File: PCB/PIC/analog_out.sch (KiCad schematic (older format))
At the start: 27 parts, among them J19 TB_1X2, Q1 PBSS5240XF, Q14 BC817-40, U18 LM358, U21 MCP6022

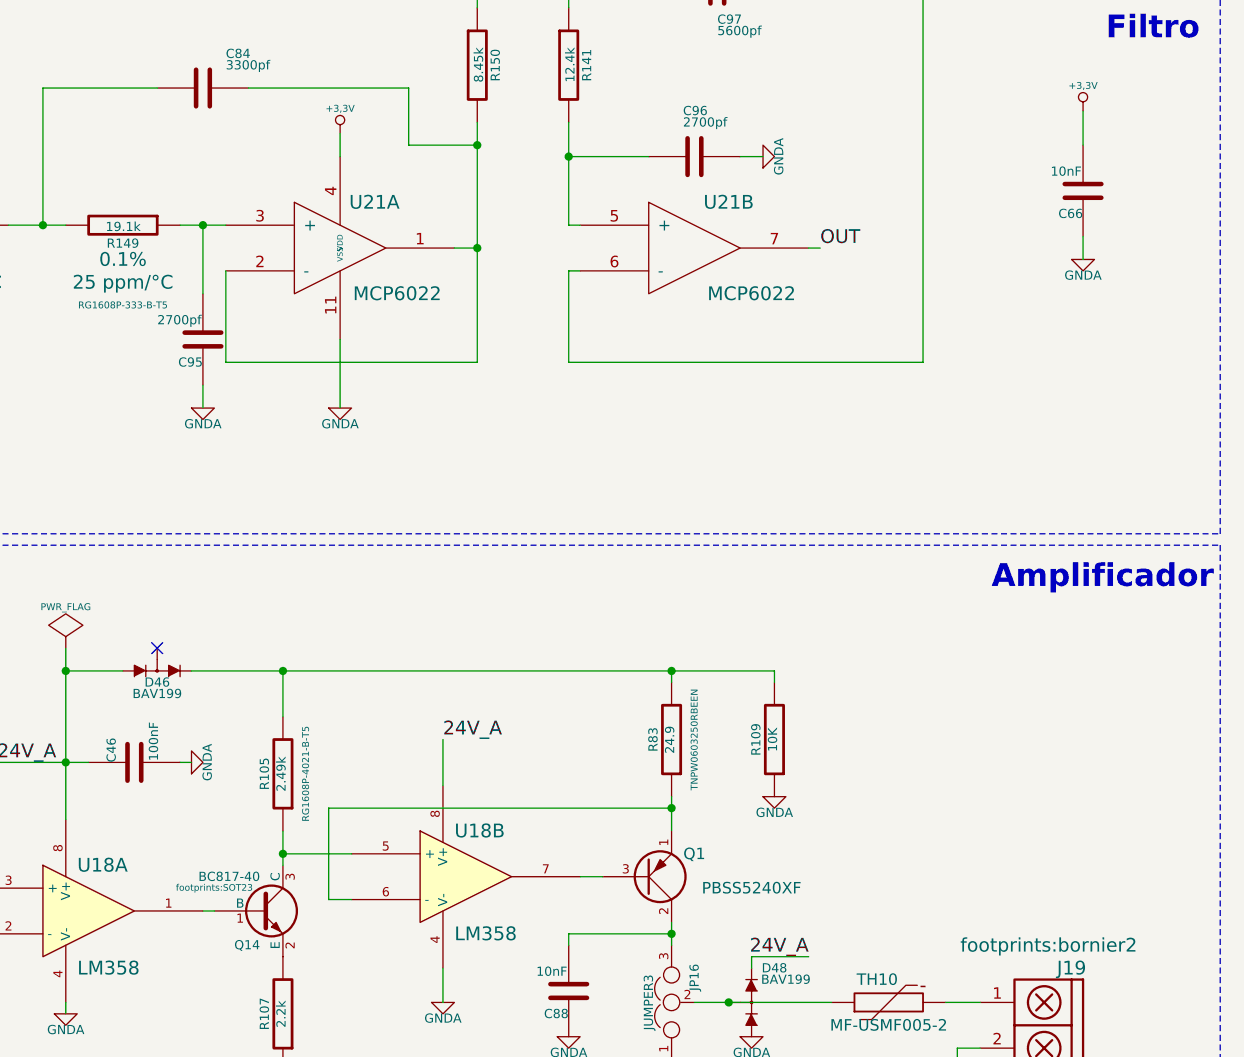
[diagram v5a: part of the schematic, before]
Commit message: rev02 se completa campo num. de frabicante(#manf) CIAA-PIC
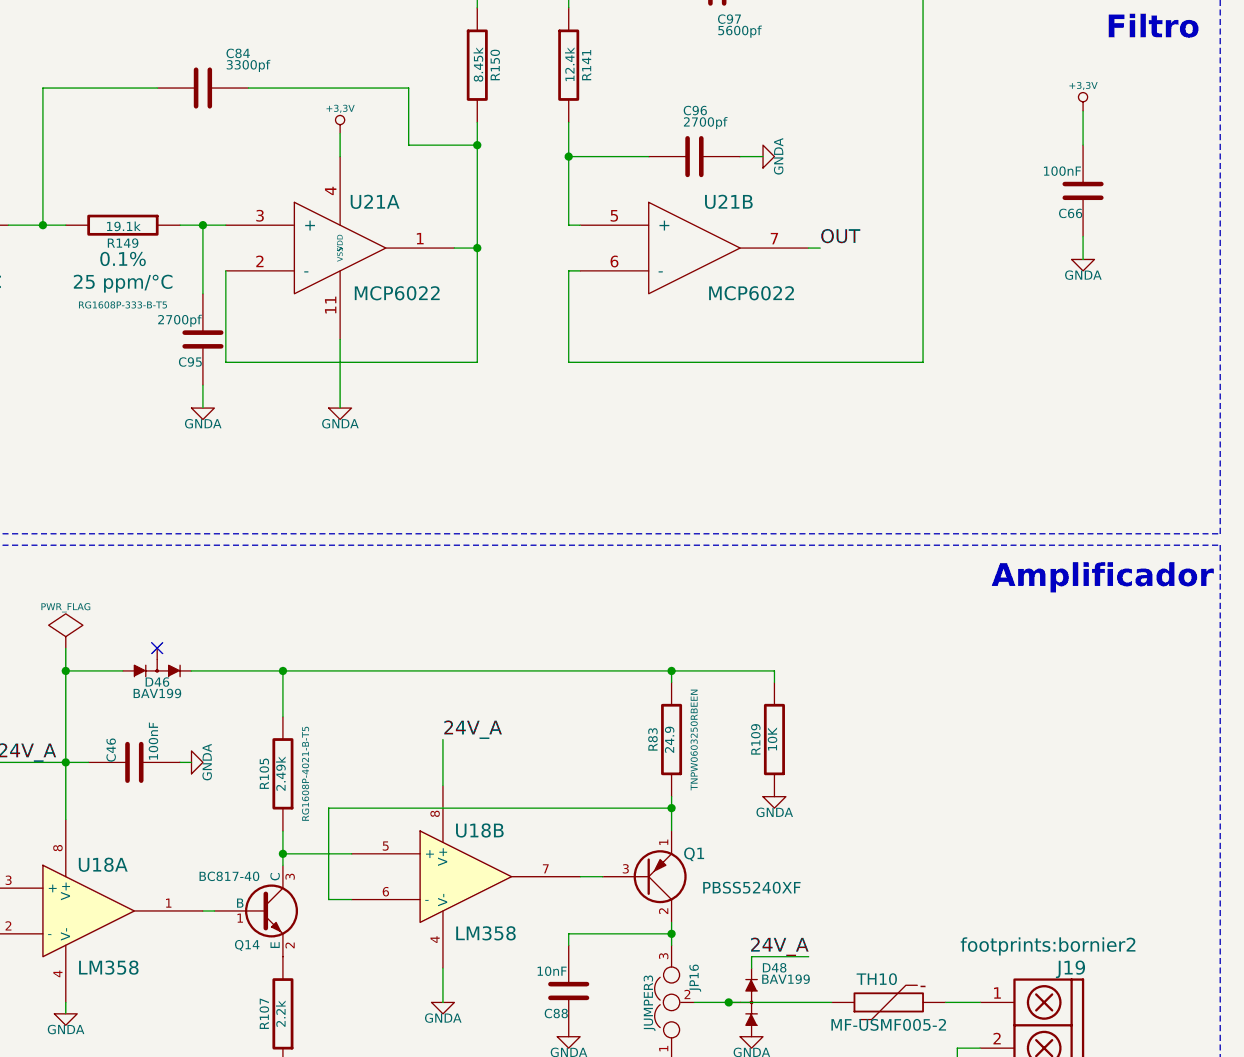
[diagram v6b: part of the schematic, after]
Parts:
- C46: #manf (none) -> C0603C104K5RACTU
- C66: value 10nF -> 100nF; #manf (none) -> C0603C104K5RACTU
- C88: #manf (none) -> C0603C103K5RACTU
- D46: footprint (none) -> footprints:SOT23-DIODE; #manf (none) -> BAV199LT1G
- D48: footprint (none) -> footprints:-SOT89; #manf (none) -> BAV199LT1G
- FB21: footprint (none) -> footprints:SM0603; #manf (none) -> MMZ1608B601CTAH0
- J19: #manf (none) -> OSTTC022162
- JP16: footprint (none) -> footprints:GS3
- Q1: footprint (none) -> footprints:-SOT89; #manf (none) -> PBSS5240XF
- Q14: #manf (none) -> BC817-40LT3G
- R105, R83: #manf (none) -> ERA-3AEB2491V
- R107: footprint Resistors_SMD:R_0603 -> Resistors_SMD:R_1206; #manf (none) -> ERJ-8GEYJ222V
- R109: #manf (none) -> RC0603JR-0710KL
- R80: #manf (none) -> ERA-3AEB333V
- R82: #manf (none) -> RG1608P-153-B-T5
- TH10: footprint (none) -> footprints:MF-USMF; #manf (none) -> MF-USMF005-2
- U18: footprint (none) -> SMD_Packages:SOIC-8-N; #manf (none) -> LM358DG
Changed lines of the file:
@@
 $EndDescr
 $Comp
-L +24V #PWR0157
+L +24V #PWR0158
 U 1 1 532CCE3B
 P 3600 4150
-F 0 "#PWR0157" H 3600 4100 20  0001 C CNN
+F 0 "#PWR0158" H 3600 4100 20  0001 C CNN
 F 1 "+24V" H 3600 4250 30  0000 C CNN
 F 2 "" H 3600 4150 60  0000 C CNN
@@
 F 2 "Capacitors_SMD:C_0603" H 5038 4050 30  0001 C CNN
 F 3 "~" H 5000 4200 60  0000 C CNN
+F 4 "C0603C104K5RACTU" H 5000 4200 60  0001 C CNN "#manf"
 	1    5000 4200
 	0    -1   -1   0
 $EndComp
 $Comp
-L GNDA-RESCUE-ciaa-pic #PWR0158
+L GNDA-RESCUE-ciaa-pic #PWR0159
 U 1 1 532CFB46
 P 4700 5300
-F 0 "#PWR0158" H 4700 5300 40  0001 C CNN
+F 0 "#PWR0159" H 4700 5300 40  0001 C CNN
 F 1 "GNDA" H 4700 5230 40  0000 C CNN
 F 2 "" H 4700 5300 60  0000 C CNN
@@
 $EndComp
 $Comp
-L GNDA-RESCUE-ciaa-pic #PWR0159
+L GNDA-RESCUE-ciaa-pic #PWR0160
 U 1 1 532CFB6F
 P 5250 4200
-F 0 "#PWR0159" H 5250 4200 40  0001 C CNN
+F 0 "#PWR0160" H 5250 4200 40  0001 C CNN
 F 1 "GNDA" H 5250 4130 40  0000 C CNN
 F 2 "" H 5250 4200 60  0000 C CNN
@@
 F 4 "0.1%" V 4900 5600 60  0000 C CNN "Tol"
 F 5 "25 ppm/°C" V 5000 5600 60  0000 C CNN "TC"
+F 6 "ERA-3AEB333V" V 4750 5600 60  0001 C CNN "#manf"
 	1    4750 5600
 	0    1    1    0
@@
 F 4 "0.1%" V 4150 5950 60  0000 C CNN "Tol"
 F 5 "25 ppm/°C" V 4250 5950 60  0000 C CNN "TC"
+F 6 "RG1608P-153-B-T5" V 4000 5950 60  0001 C CNN "#manf"
 	1    4000 5950
 	-1   0    0    1
 $EndComp
 $Comp
-L GNDA-RESCUE-ciaa-pic #PWR0160
+L GNDA-RESCUE-ciaa-pic #PWR0161
 U 1 1 532D06E5
 P 4000 6250
-F 0 "#PWR0160" H 4000 6250 40  0001 C CNN
+F 0 "#PWR0161" H 4000 6250 40  0001 C CNN
 F 1 "GNDA" H 4000 6180 40  0000 C CNN
 F 2 "" H 4000 6250 60  0000 C CNN
@@
 F 0 "U18" H 4750 5050 60  0000 L CNN
 F 1 "LM358" H 4750 4600 60  0000 L CNN
-F 2 "" H 4800 4850 60  0001 C CNN
+F 2 "SMD_Packages:SOIC-8-N" H 4800 4850 60  0001 C CNN
 F 3 "" H 4800 4850 60  0000 C CNN
+F 4 "LM358DG " H 4800 4850 60  0001 C CNN "#manf"
 	1    4800 4850
 	1    0    0    -1
@@
 F 2 "footprints:bornier2" H 9100 5700 60  0000 C CNN
 F 3 "~" H 9000 5400 60  0000 C CNN
+F 4 "OSTTC022162" H 9050 5350 60  0001 C CNN "#manf"
 	1    9050 5350
 	-1   0    0    -1
 $EndComp
 $Comp
-L GNDA-RESCUE-ciaa-pic #PWR0161
+L GNDA-RESCUE-ciaa-pic #PWR0162
 U 1 1 532A8008
 P 8600 5500
-F 0 "#PWR0161" H 8600 5500 40  0001 C CNN
+F 0 "#PWR0162" H 8600 5500 40  0001 C CNN
 F 1 "GNDA" H 8600 5430 40  0000 C CNN
 F 2 "" H 8600 5500 60  0000 C CNN
@@
 F 0 "FB21" H 4000 4350 60  0000 C CNN
 F 1 "MMZ1608B601C" H 4000 4100 60  0000 C CNN
-F 2 "" H 4000 4200 60  0001 C CNN
+F 2 "footprints:SM0603" H 4000 4200 60  0001 C CNN
 F 3 "~" H 4000 4200 60  0000 C CNN
+F 4 "MMZ1608B601CTAH0" H 4000 4200 60  0001 C CNN "#manf"
 	1    4000 4200
 	1    0    0    -1
 $EndComp
 $Comp
-L PWR_FLAG #FLG0162
+L PWR_FLAG #FLG0163
 U 1 1 532B208A
 P 4700 3700
-F 0 "#FLG0162" H 4700 3795 30  0001 C CNN
+F 0 "#FLG0163" H 4700 3795 30  0001 C CNN
 F 1 "PWR_FLAG" H 4700 3880 30  0000 C CNN
 F 2 "" H 4700 3700 60  0000 C CNN
@@
 F 0 "Q14" H 5550 4701 40  0000 R CNN
 F 1 "BC817-40" H 5550 5000 40  0000 R CNN
-F 2 "footprints:SOT23" H 5350 4952 29  0000 C CNN
+F 2 "footprints:SOT23" H 5350 4952 29  0001 C CNN
 F 3 "~" H 5550 4850 60  0000 C CNN
+F 4 "BC817-40LT3G" H 5550 4850 60  0001 C CNN "#manf"
 	1    5550 4850
 	1    0    0    -1
@@
 F 0 "R107" V 5730 5300 40  0000 C CNN
 F 1 "2.2k" V 5657 5301 40  0000 C CNN
-F 2 "Resistors_SMD:R_0603" V 5580 5300 30  0001 C CNN
+F 2 "Resistors_SMD:R_1206" V 5580 5300 30  0001 C CNN
 F 3 "~" H 5650 5300 30  0000 C CNN
+F 4 "ERJ-8GEYJ222V " V 5650 5300 60  0001 C CNN "#manf"
 	1    5650 5300
 	-1   0    0    1
@@
 F 2 "Resistors_SMD:R_0603" V 5580 4250 30  0001 C CNN
 F 3 "RG1608P-4021-B-T5" V 5550 4250 30  0000 C CNN
+F 4 "ERA-3AEB2491V " V 5650 4250 60  0001 C CNN "#manf"
 	1    5650 4250
 	-1   0    0    1
@@
 F 2 "Resistors_SMD:R_0603" V 7280 4100 30  0001 C CNN
 F 3 "TNPW0603250RBEEN" V 7250 4100 30  0000 C CNN
+F 4 "ERA-3AEB2491V " V 7350 4100 60  0001 C CNN "#manf"
 	1    7350 4100
 	-1   0    0    1
@@
 F 0 "JP16" H 7400 5150 40  0000 L CNN
 F 1 "JUMPER3" H 7350 5350 40  0000 C CNN
-F 2 "" H 7350 5250 60  0001 C CNN
+F 2 "footprints:GS3" H 7350 5250 60  0001 C CNN
 F 3 "~" H 7350 5250 60  0000 C CNN
 	1    7350 5250
@@
 F 2 "Resistors_SMD:R_0603" V 7730 4100 30  0001 C CNN
 F 3 "~" H 7800 4100 30  0000 C CNN
+F 4 "RC0603JR-0710KL" V 7800 4100 60  0001 C CNN "#manf"
 	1    7800 4100
 	-1   0    0    1
 $EndComp
 $Comp
-L GNDA-RESCUE-ciaa-pic #PWR0163
+L GNDA-RESCUE-ciaa-pic #PWR0164
 U 1 1 532CECA5
 P 7800 4350
-F 0 "#PWR0163" H 7800 4350 40  0001 C CNN
+F 0 "#PWR0164" H 7800 4350 40  0001 C CNN
 F 1 "GNDA" H 7800 4280 40  0000 C CNN
 F 2 "" H 7800 4350 60  0000 C CNN
@@
 F 0 "D48" V 7850 5150 40  0000 C CNN
 F 1 "BAV199" V 7800 5100 40  0000 C CNN
-F 2 "" H 7700 5250 60  0001 C CNN
+F 2 "footprints:-SOT89" H 7700 5250 60  0001 C CNN
 F 3 "" H 7700 5250 60  0000 C CNN
+F 4 "BAV199LT1G " V 7700 5250 60  0001 C CNN "#manf"
 	1    7700 5250
 	0    -1   -1   0
 $EndComp
 $Comp
-L GNDA-RESCUE-ciaa-pic #PWR0164
+L GNDA-RESCUE-ciaa-pic #PWR0165
 U 1 1 532CF8E2
 P 7700 5400
-F 0 "#PWR0164" H 7700 5400 40  0001 C CNN
+F 0 "#PWR0165" H 7700 5400 40  0001 C CNN
 F 1 "GNDA" H 7700 5330 40  0000 C CNN
 F 2 "" H 7700 5400 60  0000 C CNN
@@
 F 2 "Capacitors_SMD:C_0603" H 6938 5050 30  0001 C CNN
 F 3 "~" H 6900 5200 60  0000 C CNN
+F 4 "C0603C103K5RACTU " H 6900 5200 60  0001 C CNN "#manf"
 	1    6900 5200
 	-1   0    0    1
 $EndComp
 $Comp
-L GNDA-RESCUE-ciaa-pic #PWR0165
+L GNDA-RESCUE-ciaa-pic #PWR0166
 U 1 1 532CF93A
 P 6900 5400
-F 0 "#PWR0165" H 6900 5400 40  0001 C CNN
+F 0 "#PWR0166" H 6900 5400 40  0001 C CNN
 F 1 "GNDA" H 6900 5330 40  0000 C CNN
 F 2 "" H 6900 5400 60  0000 C CNN
@@
 F 0 "D46" H 5100 3750 40  0000 C CNN
 F 1 "BAV199" H 5100 3700 40  0000 C CNN
-F 2 "" H 5100 3800 60  0001 C CNN
+F 2 "footprints:SOT23-DIODE" H 5100 3800 60  0001 C CNN
 F 3 "" H 5100 3800 60  0000 C CNN
+F 4 "BAV199LT1G " H 5100 3800 60  0001 C CNN "#manf"
 	1    5100 3800
 	1    0    0    -1
@@
 F 0 "TH10" V 8400 5300 50  0000 C CNN
 F 1 "MF-USMF005-2" V 8200 5250 50  0000 C CNN
-F 2 "" H 8300 5250 60  0001 C CNN
+F 2 "footprints:MF-USMF" H 8300 5250 60  0001 C CNN
 F 3 "~" H 8300 5250 60  0000 C CNN
+F 4 "MF-USMF005-2" V 8300 5250 60  0001 C CNN "#manf"
 	1    8300 5250
 	0    -1   -1   0
@@
 F 0 "Q1" H 7450 4600 50  0000 C CNN
 F 1 "PBSS5240XF" H 7700 4750 50  0000 C CNN
-F 2 "" H 7650 4650 60  0001 C CNN
+F 2 "footprints:-SOT89" H 7650 4650 60  0001 C CNN
 F 3 "~" H 7250 4700 60  0000 C CNN
+F 4 "PBSS5240XF" H 7250 4700 60  0001 C CNN "#manf"
 	1    7250 4700
 	1    0    0    1
@@
 P 9150 1700
 F 0 "C66" H 9150 1800 40  0000 L CNN
-F 1 "10nF" H 9156 1615 40  0000 L CNN
+F 1 "100nF" H 9156 1615 40  0000 L CNN
 F 2 "Capacitors_SMD:C_0603" H 9188 1550 30  0001 C CNN
 F 3 "~" H 9150 1700 60  0000 C CNN
+F 4 "C0603C104K5RACTU" H 9150 1700 60  0001 C CNN "#manf"
 	1    9150 1700
 	-1   0    0    1
 $EndComp
 $Comp
-L GNDA-RESCUE-ciaa-pic #PWR0166
+L GNDA-RESCUE-ciaa-pic #PWR0167
 U 1 1 53BAF7F5
 P 9150 2000
-F 0 "#PWR0166" H 9150 2000 40  0001 C CNN
+F 0 "#PWR0167" H 9150 2000 40  0001 C CNN
 F 1 "GNDA" H 9150 1930 40  0000 C CNN
 F 2 "" H 9150 2000 60  0000 C CNN
@@
 Ver AN538, AN655 Microchip\nMPLAB Started Kit for dsPIC (Fig A-6) \n
 $Comp
-L GNDA-RESCUE-ciaa-pic #PWR0167
+L GNDA-RESCUE-ciaa-pic #PWR0168
 U 1 1 53BB004F
 P 6350 5250
-F 0 "#PWR0167" H 6350 5250 40  0001 C CNN
+F 0 "#PWR0168" H 6350 5250 40  0001 C CNN
 F 1 "GNDA" H 6350 5180 40  0000 C CNN
 F 2 "" H 6350 5250 60  0000 C CNN
@@
 $EndComp
 $Comp
-L GNDA-RESCUE-ciaa-pic #PWR0168
+L GNDA-RESCUE-ciaa-pic #PWR0169
 U 1 1 543D3CD6
 P 5300 2650
-F 0 "#PWR0168" H 5300 2650 40  0001 C CNN
+F 0 "#PWR0169" H 5300 2650 40  0001 C CNN
 F 1 "GNDA" H 5300 2580 40  0000 C CNN
 F 2 "" H 5300 2650 60  0000 C CNN
@@
 $EndComp
 $Comp
-L GNDA-RESCUE-ciaa-pic #PWR0169
+L GNDA-RESCUE-ciaa-pic #PWR0170
 U 1 1 543D3EA5
 P 7750 1550
-F 0 "#PWR0169" H 7750 1550 40  0001 C CNN
+F 0 "#PWR0170" H 7750 1550 40  0001 C CNN
 F 1 "GNDA" H 7750 1480 40  0000 C CNN
 F 2 "" H 7750 1550 60  0000 C CNN
@@
 OUT
 $Comp
-L +3,3V #PWR0170
+L +3,3V #PWR0171
 U 1 1 543D7CD7
 P 5900 1450
-F 0 "#PWR0170" H 5900 1410 30  0001 C CNN
+F 0 "#PWR0171" H 5900 1410 30  0001 C CNN
 F 1 "+3,3V" H 5900 1560 30  0000 C CNN
 F 2 "" H 5900 1450 60  0000 C CNN
@@
 $EndComp
 $Comp
-L +3,3V #PWR0171
+L +3,3V #PWR0172
 U 1 1 543D7CE4
 P 9150 1350
-F 0 "#PWR0171" H 9150 1310 30  0001 C CNN
+F 0 "#PWR0172" H 9150 1310 30  0001 C CNN
 F 1 "+3,3V" H 9150 1460 30  0000 C CNN
 F 2 "" H 9150 1350 60  0000 C CNN
@@
 $EndComp
 $Comp
-L GNDA-RESCUE-ciaa-pic #PWR0172
+L GNDA-RESCUE-ciaa-pic #PWR0173
 U 1 1 543D7CEA
 P 5900 2650
-F 0 "#PWR0172" H 5900 2650 40  0001 C CNN
+F 0 "#PWR0173" H 5900 2650 40  0001 C CNN
 F 1 "GNDA" H 5900 2580 40  0000 C CNN
 F 2 "" H 5900 2650 60  0000 C CNN
@@
 Wire Wire Line
 	7450 5250 8050 5250
-Connection ~ 7600 5250
 Wire Wire Line
 	7950 5050 7700 5050
@@
 Text Notes 8750 3450 0    99   ~ 20
 Amplificador
+Connection ~ 7600 5250
 $EndSCHEMATC
